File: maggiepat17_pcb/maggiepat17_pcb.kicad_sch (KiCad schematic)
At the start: 55 parts, among them J1 USB_C_Receptacle, J2 AudioJack4, J3 Conn_01x03_Male, J4 Conn_01x03_Male, J5 TP1, J6 TP2, J7 TP3, SW1 SW_Push, SW10 RESET, SW2 SW_Push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

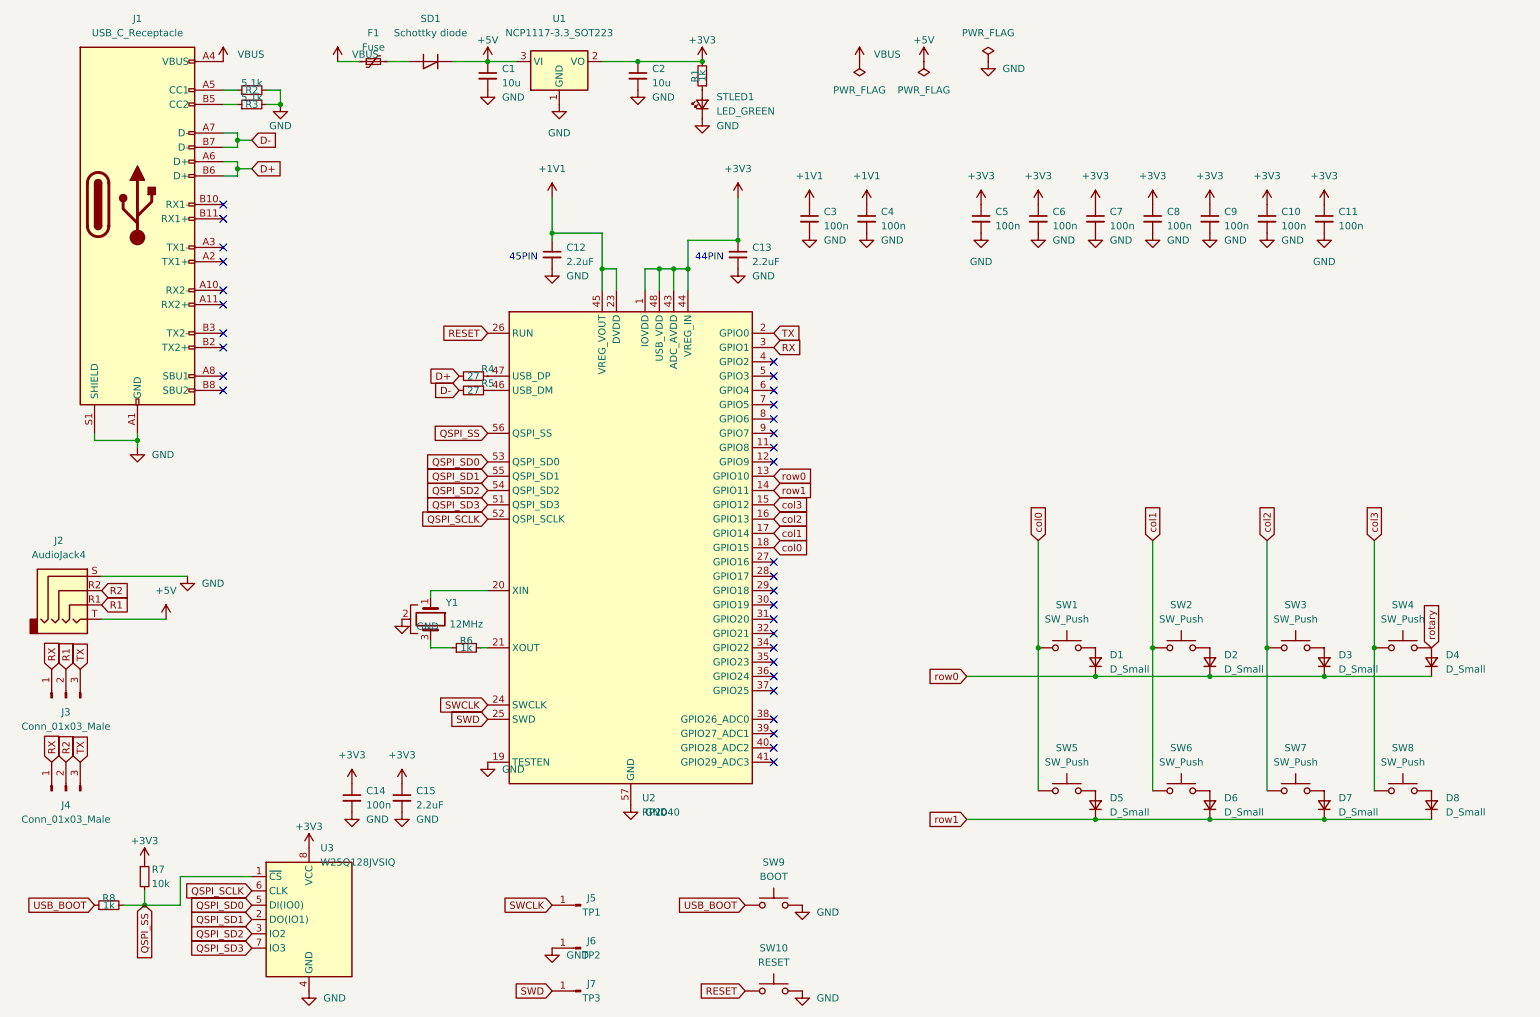
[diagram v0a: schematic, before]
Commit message: added switches
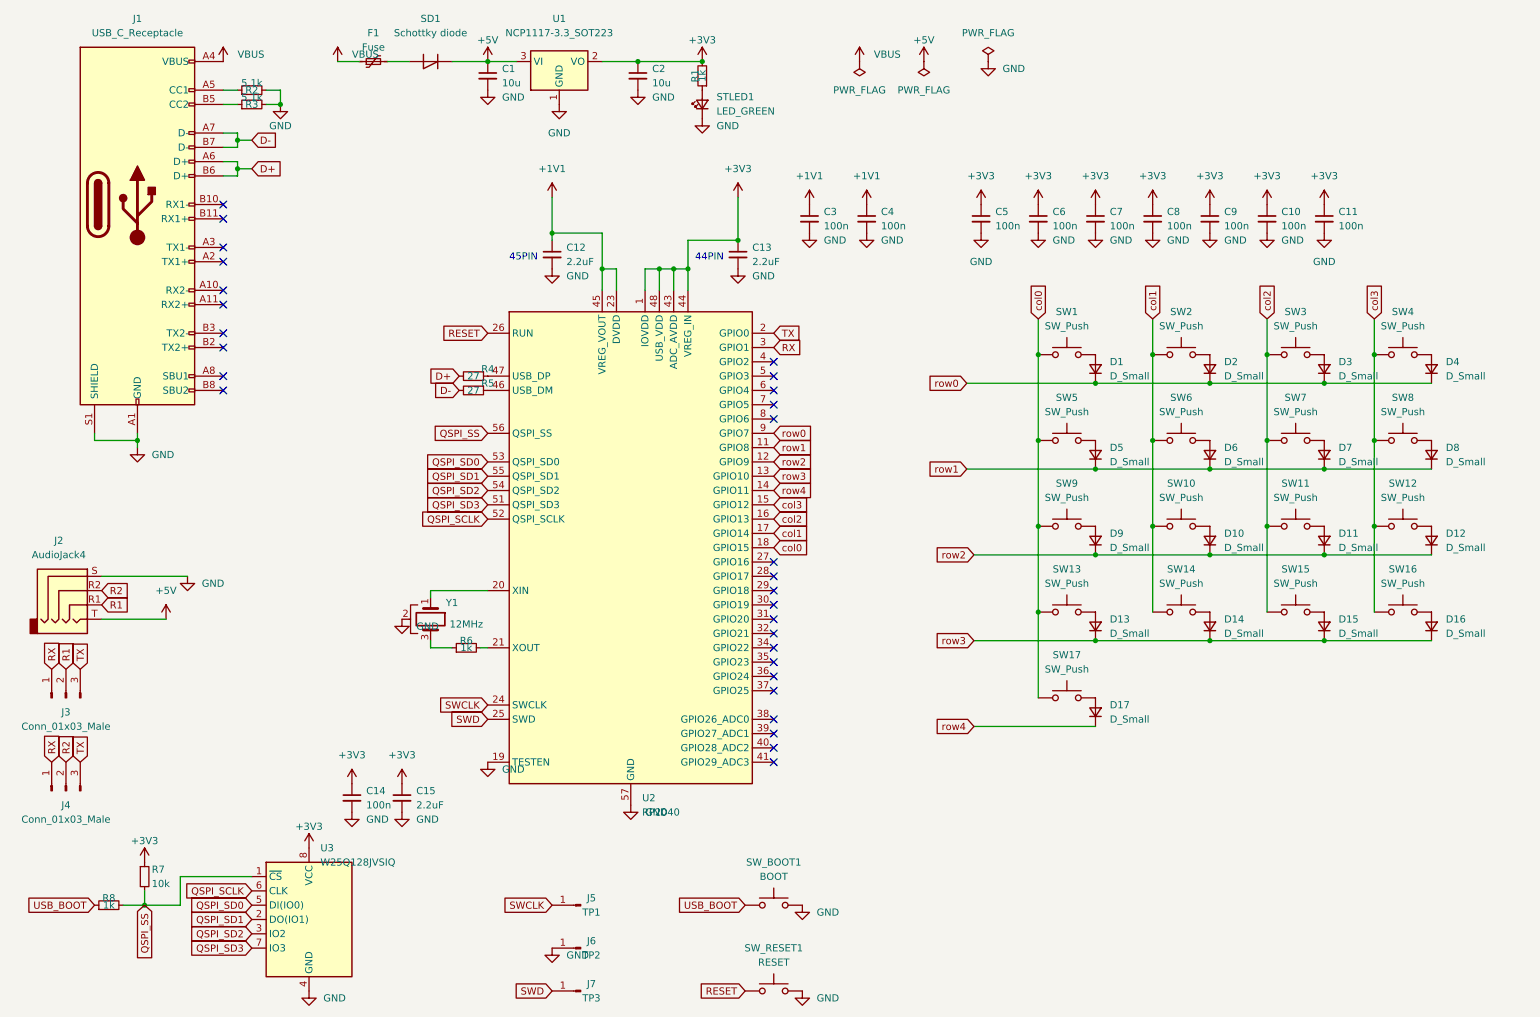
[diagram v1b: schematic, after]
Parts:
- added D10, D11, D12, D13, D14, D15, D16, D17, D9: D_Small, Diode_SMD:D_SOD-123, symbol Device:D_Small
- added SW10, SW11, SW12, SW13, SW14, SW15, SW16, SW17, SW9: SW_Push, Button_Switch_Keyboard:SW_Cherry_MX_1.00u_PCB, symbol Switch:SW_Push
- renumbered SW9 to SW_BOOT1, SW10 to SW_RESET1
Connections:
- net col0: now also SW13.1, SW17.1, SW9.1
- net col1: now also SW10.1, SW14.1
- net col2: now also SW11.1, SW15.1
- net col3: now also SW12.1, SW16.1
- net row0: now also U2.9 (GPIO7); no longer U2.13 (GPIO10)
- net row1: now also U2.11 (GPIO8); no longer U2.14 (GPIO11)
- net row2: now reaches U2.12 (GPIO9)
- net row2: now also D10.1 (K), D11.1 (K), D12.1 (K), D9.1 (K)
- net rotary: no longer names the net of D4.2 (A), SW4.2
- new net: D12.2 (A), SW12.2
- new net: D17.2 (A), SW17.2
- new net: D13.2 (A), SW13.2
- new net: D10.2 (A), SW10.2
- new net: D16.2 (A), SW16.2
- new net: D15.2 (A), SW15.2
- new net: D14.2 (A), SW14.2
- new net: D11.2 (A), SW11.2
- new net: D9.2 (A), SW9.2
- new net row3: D13.1 (K), D14.1 (K), D15.1 (K), D16.1 (K), U2.13 (GPIO10)
- new net row4: D17.1 (K), U2.14 (GPIO11)
- no-connect marks 32 -> 29
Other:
- moved on the sheet: D1, D2, D3, D4, D5, D6, D7, D8, SW1, SW2, SW3, SW4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

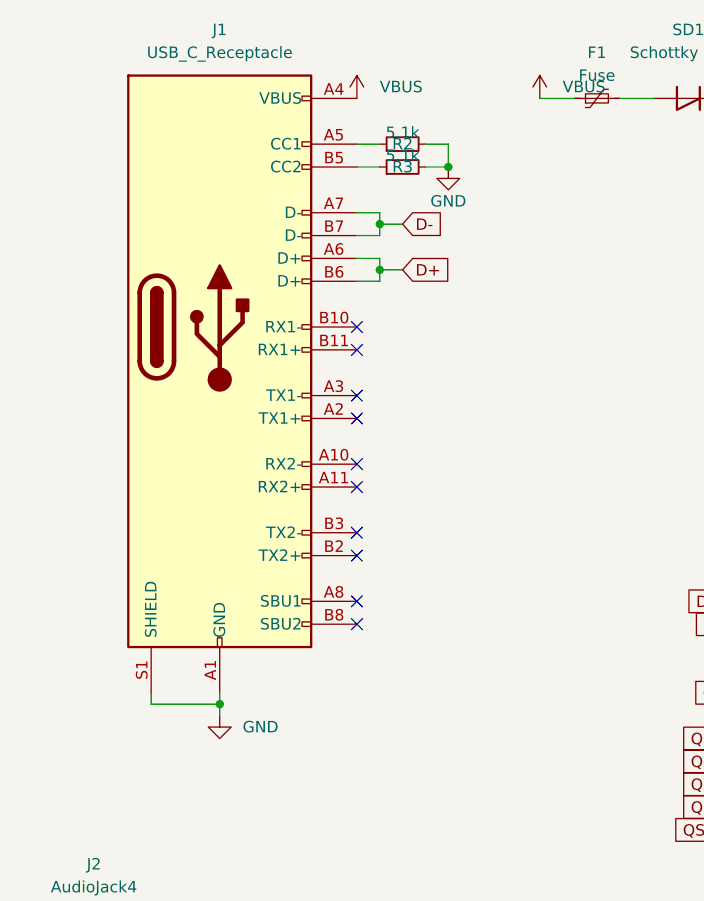
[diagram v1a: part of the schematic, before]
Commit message: changed USB connector
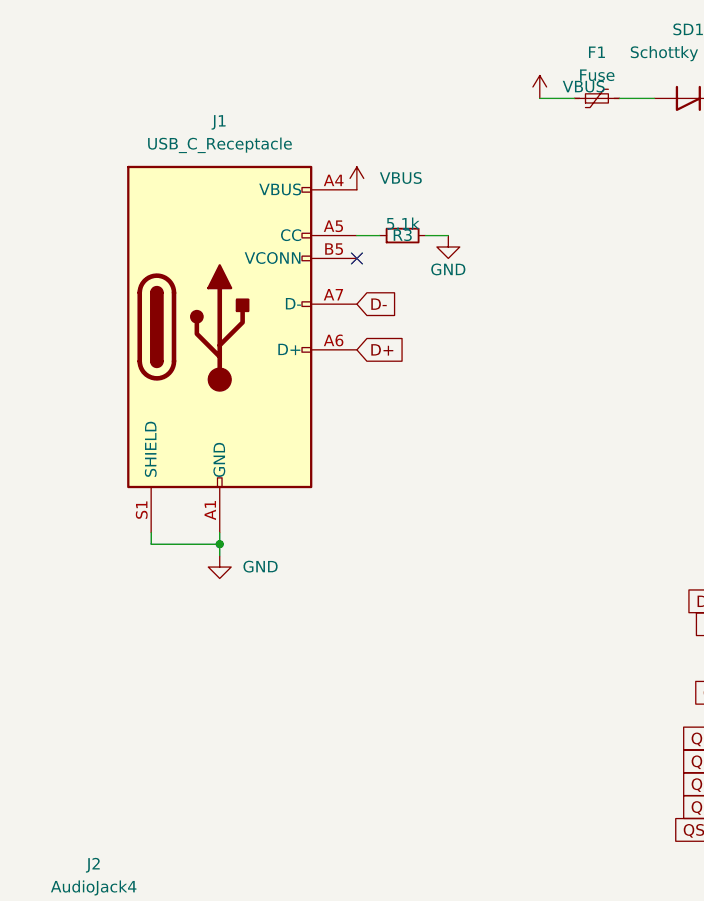
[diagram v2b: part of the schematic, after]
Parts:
- removed R2: 5.1k, Resistor_SMD:R_0402_1005Metric, symbol Device:R_Small
- J1: symbol Connector:USB_C_Receptacle -> Connector:USB_C_Plug_USB2.0
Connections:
- net D+: no longer J1.B6 (D+)
- net D-: no longer J1.B7 (D-)
- net at J1.A5 (CC): now also R3.1
- net at J1.B5 (VCONN): no longer R3.1
- no-connect marks 29 -> 20
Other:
- moved on the sheet: R3

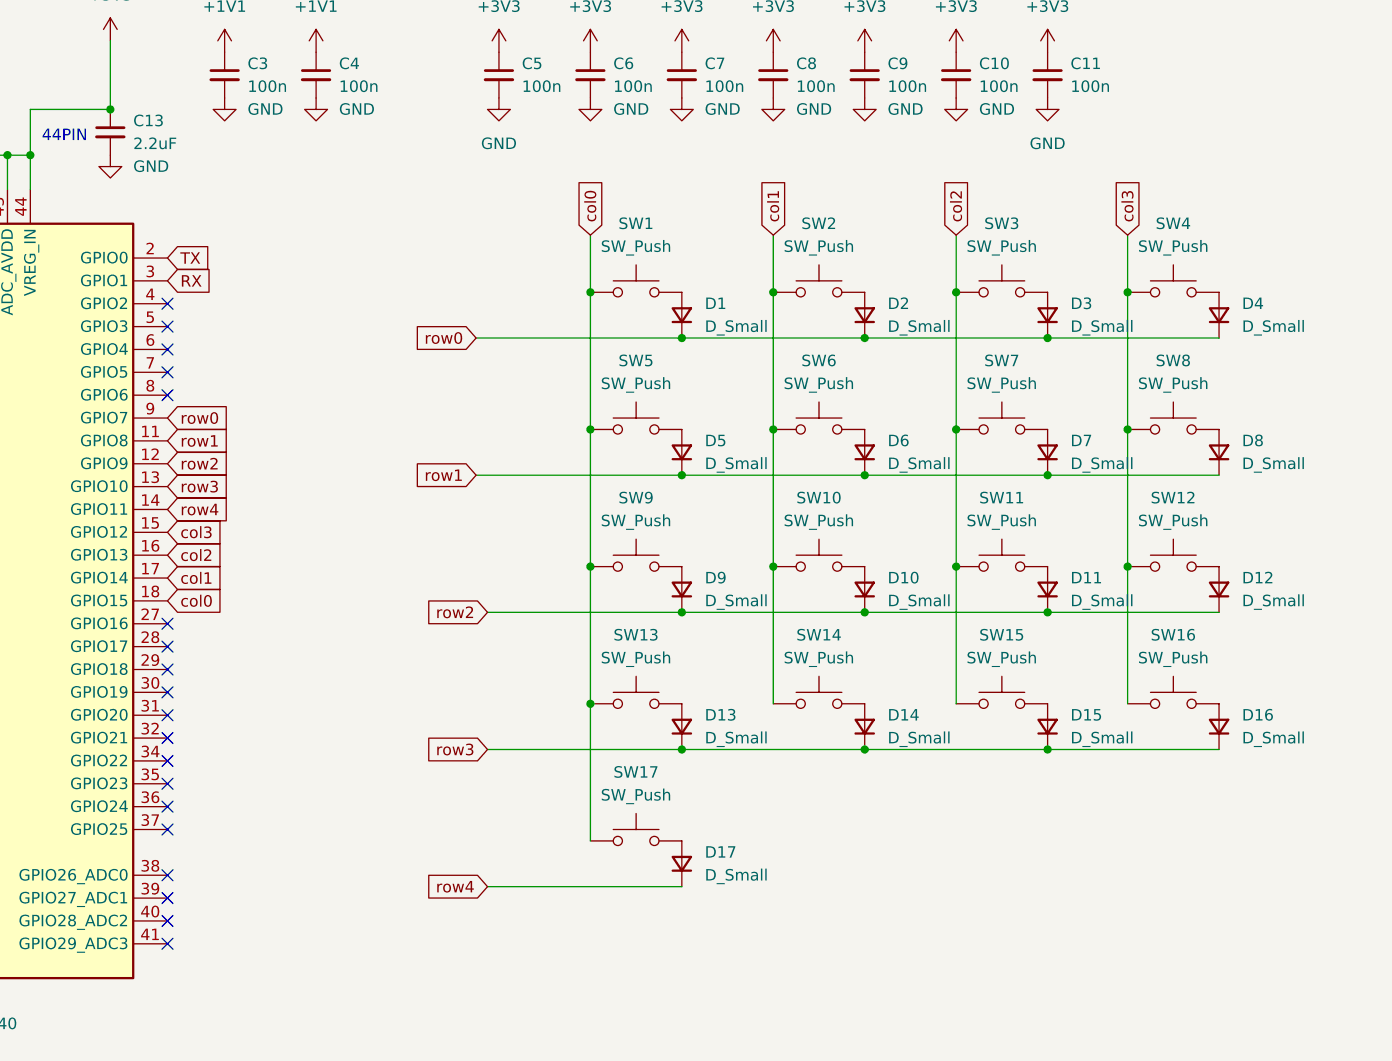
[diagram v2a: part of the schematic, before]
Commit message: fixed switch metrix
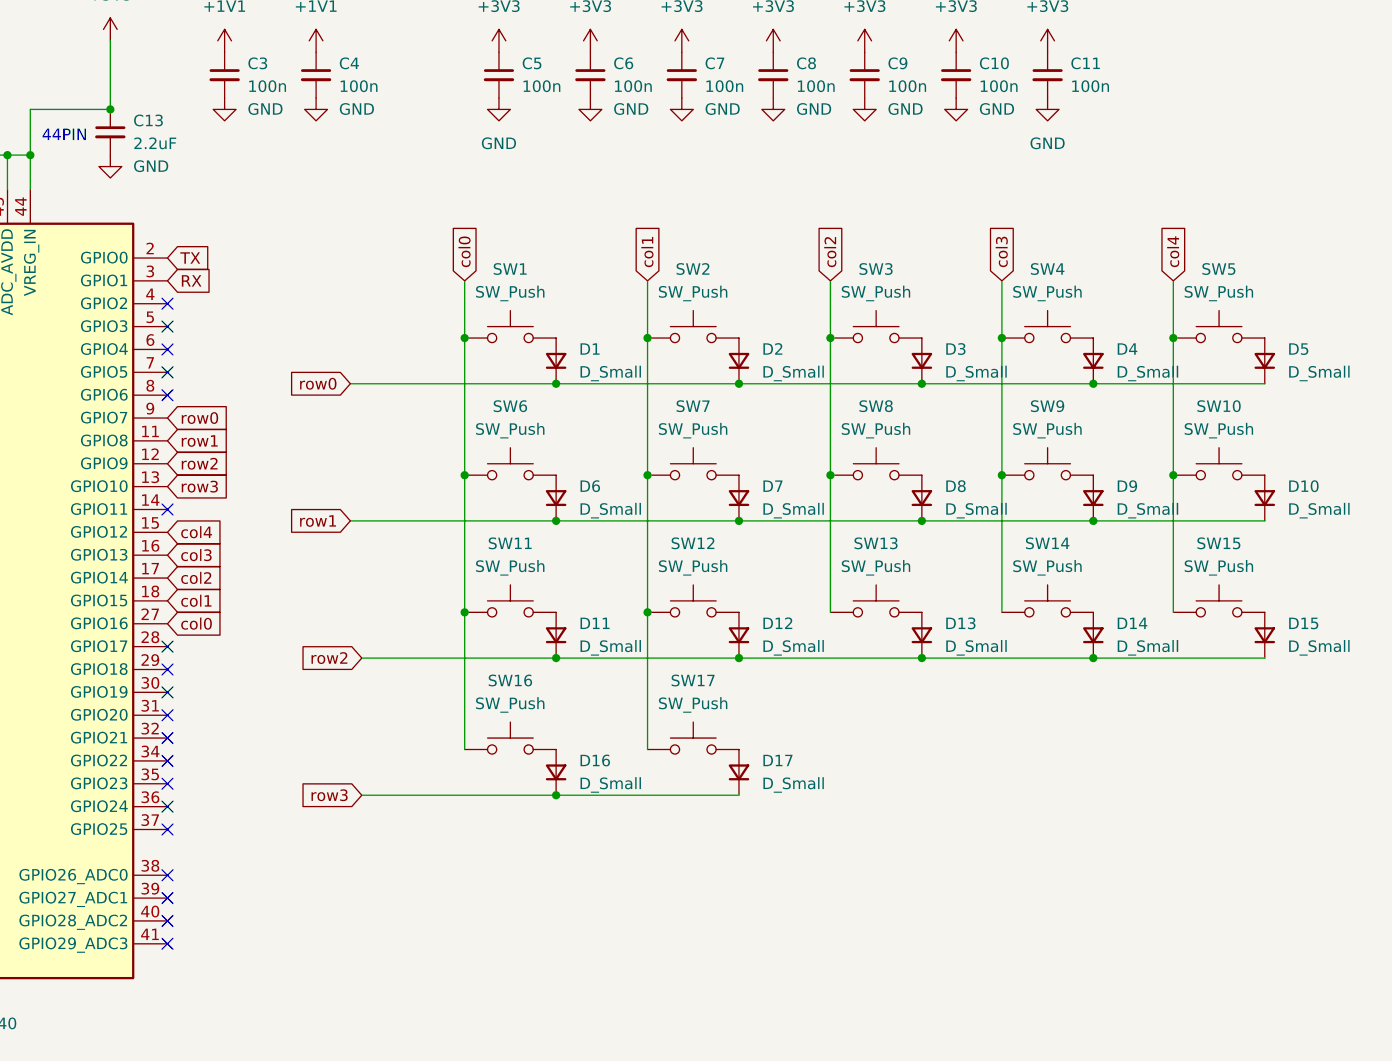
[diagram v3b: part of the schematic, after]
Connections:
- net col0: now also SW11.1, SW16.1, SW6.1, U2.27 (GPIO16); no longer SW13.1, SW17.1, SW5.1, SW9.1, U2.18 (GPIO15)
- net col1: now also SW12.1, SW17.1, SW7.1, U2.18 (GPIO15); no longer SW10.1, SW14.1, SW6.1, U2.17 (GPIO14)
- net col2: now also SW13.1, SW8.1, U2.17 (GPIO14); no longer SW11.1, SW15.1, SW7.1, U2.16 (GPIO13)
- net col3: now also SW14.1, SW9.1, U2.16 (GPIO13); no longer SW12.1, SW16.1, SW8.1, U2.15 (GPIO12)
- net row0: now also D5.1 (K)
- net row1: now also D10.1 (K), D9.1 (K); no longer D5.1 (K)
- net row2: now also D13.1 (K), D14.1 (K), D15.1 (K); no longer D10.1 (K), D9.1 (K)
- net row3: now also D17.1 (K); no longer D13.1 (K), D14.1 (K), D15.1 (K)
- net row4: no longer names the net of U2.14 (GPIO11)
- net row4: no longer D17.1 (K)
- new net col4: SW10.1, SW15.1, SW5.1, U2.15 (GPIO12)
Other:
- moved on the sheet: D1, D10, D11, D12, D13, D14, D15, D16, D17, D2, D3, D4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

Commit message: created PCBA order files, need to replace
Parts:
- removed J2: AudioJack4, Connector_Audio:Jack_3.5mm_KoreanHropartsElec_PJ-320D-4A_Horizontal, symbol Connector_Audio:AudioJack4
- removed J3, J4: Conn_01x03_Male, Jumper:SolderJumper-3_P1.3mm_Open_Pad1.0x1.5mm_NumberLabels, symbol Connector:Conn_01x03_Pin
- added R2: 5.1k, Resistor_SMD:R_0402_1005Metric, symbol Device:R_Small
- J1: symbol Connector:USB_C_Plug_USB2.0 -> Connector:USB_C_Receptacle_USB2.0_16P
- SW1, SW10, SW11, SW12, SW13, SW14, SW15, SW16, SW17, SW2, SW3, SW4, SW5, SW6, SW7, SW8, SW9: footprint Button_Switch_Keyboard:SW_Cherry_MX_1.00u_PCB -> kbd:keyswitch_cherrymx_hotswap_1u
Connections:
- net D+: now also J1.B6 (D+)
- net D-: now also J1.B7 (D-)
- net GND: now also R2.2
- net col0: now also U2.14 (GPIO11); no longer SW16.1, U2.27 (GPIO16)
- net col1: now also U2.15 (GPIO12); no longer SW17.1, U2.18 (GPIO15)
- net col2: now also U2.16 (GPIO13); no longer U2.17 (GPIO14)
- net col3: now also SW16.1, U2.17 (GPIO14); no longer U2.16 (GPIO13)
- net col4: now also SW17.1, U2.18 (GPIO15); no longer U2.15 (GPIO12)
- net row0: now also U2.4 (GPIO2); no longer U2.9 (GPIO7)
- net row1: now also U2.5 (GPIO3); no longer U2.11 (GPIO8)
- net row2: now also U2.6 (GPIO4); no longer U2.12 (GPIO9)
- net row3: now also U2.7 (GPIO5); no longer U2.13 (GPIO10)
- net at J1.B5 (CC2): now also R2.1
- net RX: no longer names the net of U2.3 (GPIO1)
- net TX: no longer names the net of U2.2 (GPIO0)
- no-connect marks 20 -> 23
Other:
- moved on the sheet: D16, D17, SW16, SW17

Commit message: updated bom files, order passed
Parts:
- C1, C2: LCSC (none) -> C13585
- C12, C13, C15: LCSC (none) -> C12530
- C14: LCSC (none) -> C1525
- J1: LCSC (none) -> C165948
- R1: LCSC (none) -> C11702
- R2, R3: LCSC (none) -> C25905
- R4, R5: LCSC (none) -> C25100
- R7: LCSC (none) -> C25744
- SD1: LCSC (none) -> C8598
- STLED1: LCSC (none) -> C130723
- U1: LCSC (none) -> C347222
- U3: LCSC (none) -> C190862
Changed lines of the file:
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@@
 			)
 		)
+		(property "LCSC" "C12530"
+			(at 142.24 57.15 0)
+			(effects
+				(font
+					(size 1.27 1.27)
+				)
+				(hide yes)
+			)
+		)
 		(pin "1"
 		)
@@
 			)
 		)
+		(property "LCSC" "C25100"
+			(at 95.25 78.74 90)
+			(effects
+				(font
+					(size 1.27 1.27)
+				)
+				(hide yes)
+			)
+		)
 		(pin "1"
 		)
@@
 			)
 		)
+		(property "LCSC" "C1525"
+			(at 73.66 153.67 0)
+			(effects
+				(font
+					(size 1.27 1.27)
+				)
+				(hide yes)
+			)
+		)
 		(pin "1"
 		)
@@
 			)
 		)
+		(property "LCSC" "C11702"
+			(at 135.89 25.4 90)
+			(effects
+				(font
+					(size 1.27 1.27)
+				)
+				(hide yes)
+			)
+		)
 		(pin "1"
 		)
@@
 			)
 		)
+		(property "LCSC" "C25905"
+			(at 55.88 40.64 90)
+			(effects
+				(font
+					(size 1.27 1.27)
+				)
+				(hide yes)
+			)
+		)
 		(pin "1"
 		)
@@
 			)
 		)
+		(property "LCSC" "C12530"
+			(at 109.22 57.15 0)
+			(effects
+				(font
+					(size 1.27 1.27)
+				)
+				(hide yes)
+			)
+		)
 		(pin "1"
 		)
@@
 			)
 		)
+		(property "LCSC" "C347222"
+			(at 110.49 22.86 0)
+			(effects
+				(font
+					(size 1.27 1.27)
+				)
+				(hide yes)
+			)
+		)
 		(pin "1"
 		)
@@
 			)
 		)
+		(property "LCSC" "C25100"
+			(at 95.25 81.28 90)
+			(effects
+				(font
+					(size 1.27 1.27)
+				)
+				(hide yes)
+			)
+		)
 		(pin "1"
 		)
@@
 			)
 		)
+		(property "LCSC" "C130723"
+			(at 135.89 30.48 90)
+			(effects
+				(font
+					(size 1.27 1.27)
+				)
+				(hide yes)
+			)
+		)
 		(pin "1"
 		)
@@
 			)
 		)
+		(property "LCSC" "C12530"
+			(at 82.55 153.67 0)
+			(effects
+				(font
+					(size 1.27 1.27)
+				)
+				(hide yes)
+			)
+		)
 		(pin "1"
 		)
@@
 			)
 		)
+		(property "LCSC" "C25744"
+			(at 36.83 167.64 0)
+			(effects
+				(font
+					(size 1.27 1.27)
+				)
+				(hide yes)
+			)
+		)
 		(pin "1"
 		)
@@
 			)
 		)
+		(property "LCSC" "C13585"
+			(at 124.46 25.4 0)
+			(effects
+				(font
+					(size 1.27 1.27)
+				)
+				(hide yes)
+			)
+		)
 		(pin "1"
 		)
@@
 			)
 		)
+		(property "LCSC" "C190862"
+			(at 66.04 175.26 0)
+			(effects
+				(font
+					(size 1.27 1.27)
+				)
+				(hide yes)
+			)
+		)
 		(pin "1"
 		)
@@
 			)
 		)
+		(property "LCSC" "C165948"
+			(at 35.56 48.26 0)
+			(effects
+				(font
+					(size 1.27 1.27)
+				)
+				(hide yes)
+			)
+		)
 		(pin "A1"
 		)
@@
 			)
 		)
+		(property "LCSC" "C13585"
+			(at 97.79 25.4 0)
+			(effects
+				(font
+					(size 1.27 1.27)
+				)
+				(hide yes)
+			)
+		)
 		(pin "1"
 		)
@@
 			)
 		)
+		(property "LCSC" "C8598"
+			(at 87.63 22.86 0)
+			(effects
+				(font
+					(size 1.27 1.27)
+				)
+				(hide yes)
+			)
+		)
 		(pin "1"
 		)
@@
 			(effects
 				(font
+					(size 1.27 1.27)
+				)
+				(hide yes)
+			)
+		)
+		(property "LCSC" "C25905"
+			(at 55.88 38.1 90)
+			(effects
+				(font
